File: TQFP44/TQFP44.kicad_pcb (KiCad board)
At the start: 2 copper layers, 56.1 x 20.6 mm, 12 parts, among them J1 Conn_01x22, J2 Conn_01x22, J3 Conn_02x22_Counter_Clockwise, J4 Conn_02x22_Counter_Clockwise, J5 Conn_02x22_Counter_Clockwise, J6 Conn_01x06

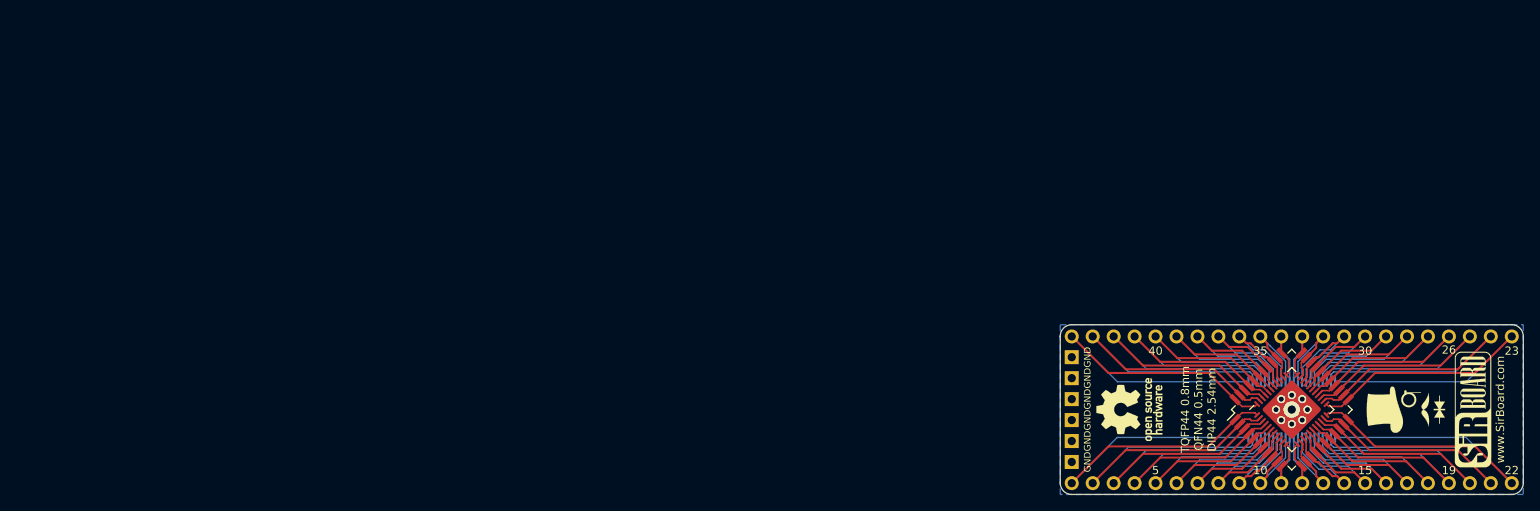
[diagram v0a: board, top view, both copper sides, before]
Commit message: USB, SD and CR Cells Added
MicroSD, MicroUSB, MiniUSB, USB-C, CR1220, CR2032 added as well as all schematics page sizes optimised
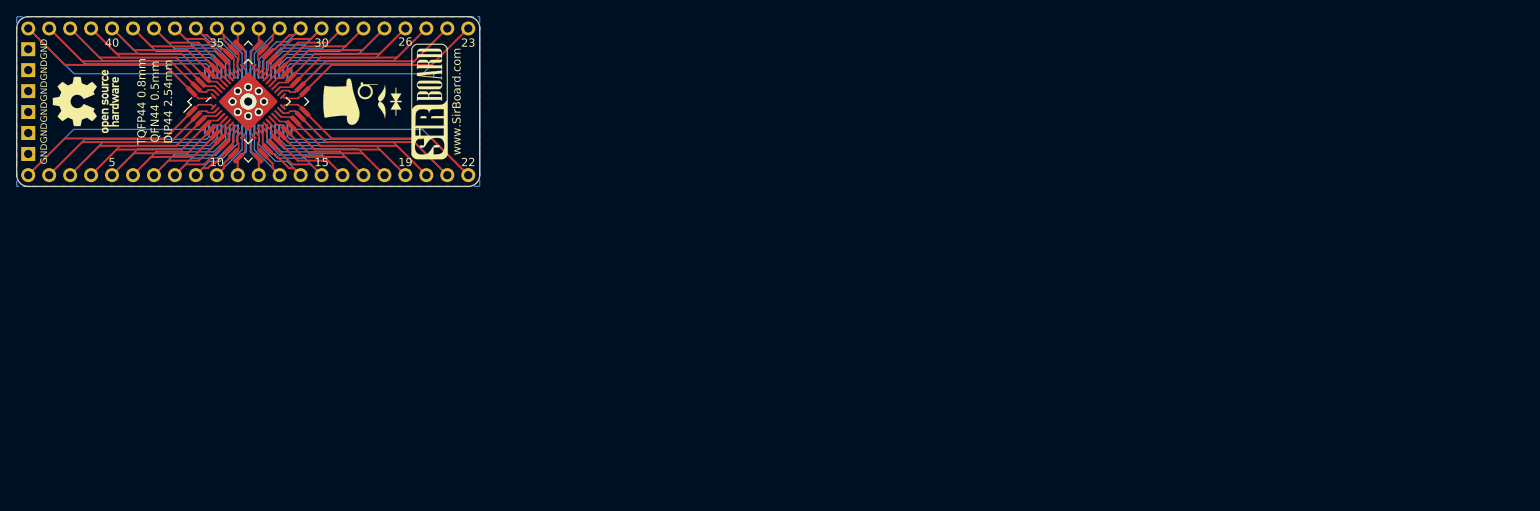
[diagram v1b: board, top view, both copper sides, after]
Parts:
- moved J3 131.9 mm to (67.9, 35.1)
- moved J5 131.9 mm to (67.9, 35.1)
- moved REF** 131.9 mm to (48.3, 35.1)
- moved G*** 131.9 mm to (81.8, 35.1)
- moved G*** 131.9 mm to (89.2, 35.1)
- moved G*** 131.9 mm to (79.4, 35.0)
- moved G*** 131.9 mm to (89.9, 35.1)
- moved J1 131.9 mm to (41.3, 26.2)
- moved J2 131.9 mm to (41.3, 44.0)
- moved J4 131.9 mm to (67.9, 35.0)
- moved J6 131.9 mm to (41.3, 41.4)
- moved REF** 131.9 mm to (50.7, 35.1)

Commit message: Board Updates
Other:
- board size 56.1 x 20.6 mm -> 55.9 x 20.3 mm
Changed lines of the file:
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@@
     (0 F.Cu signal)
     (31 B.Cu signal)
-    (32 B.Adhes user)
-    (33 F.Adhes user)
-    (34 B.Paste user)
-    (35 F.Paste user)
+    (32 B.Adhes user hide)
+    (33 F.Adhes user hide)
+    (34 B.Paste user hide)
+    (35 F.Paste user hide)
     (36 B.SilkS user)
     (37 F.SilkS user)
-    (38 B.Mask user)
-    (39 F.Mask user)
+    (38 B.Mask user hide)
+    (39 F.Mask user hide)
     (40 Dwgs.User user)
     (41 Cmts.User user hide)
@@
       (xy -6.38175 -2.199822) (xy 6.399893 -2.199822) (xy 6.472464 -2.17505)) (layer F.SilkS) (width 0.01))
   )
+  (gr_arc (start 94.615 43.942) (end 94.615 45.212) (angle -90) (layer Edge.Cuts) (width 0.05))
+  (gr_arc (start 41.275 43.942) (end 40.005 43.942) (angle -90) (layer Edge.Cuts) (width 0.05))
+  (gr_arc (start 41.275 26.162) (end 41.275 24.892) (angle -90) (layer Edge.Cuts) (width 0.05))
+  (gr_arc (start 94.615 26.162) (end 95.885 26.162) (angle -90) (layer Edge.Cuts) (width 0.05))
   (gr_text 44 (at 94.615 27.813) (layer B.SilkS)
     (effects (font (size 1 1) (thickness 0.15)) (justify mirror))
@@
     (effects (font (size 1 1) (thickness 0.15)) (justify mirror))
   )
-  (dimension 56.134 (width 0.15) (layer Dwgs.User)
-    (gr_text "56.134 mm" (at 67.945 18.6898) (layer Dwgs.User)
+  (dimension 55.88 (width 0.15) (layer Dwgs.User)
+    (gr_text "55.880 mm" (at 67.945 18.766) (layer Dwgs.User)
       (effects (font (size 1 1) (thickness 0.15)) hide)
     )
-    (feature1 (pts (xy 96.012 24.765) (xy 96.012 19.403379)))
-    (feature2 (pts (xy 39.878 24.765) (xy 39.878 19.403379)))
-    (crossbar (pts (xy 39.878 19.9898) (xy 96.012 19.9898)))
-    (arrow1a (pts (xy 96.012 19.9898) (xy 94.885496 20.576221)))
-    (arrow1b (pts (xy 96.012 19.9898) (xy 94.885496 19.403379)))
-    (arrow2a (pts (xy 39.878 19.9898) (xy 41.004504 20.576221)))
-    (arrow2b (pts (xy 39.878 19.9898) (xy 41.004504 19.403379)))
+    (feature1 (pts (xy 95.885 26.162) (xy 95.885 19.479579)))
+    (feature2 (pts (xy 40.005 26.162) (xy 40.005 19.479579)))
+    (crossbar (pts (xy 40.005 20.066) (xy 95.885 20.066)))
+    (arrow1a (pts (xy 95.885 20.066) (xy 94.758496 20.652421)))
+    (arrow1b (pts (xy 95.885 20.066) (xy 94.758496 19.479579)))
+    (arrow2a (pts (xy 40.005 20.066) (xy 41.131504 20.652421)))
+    (arrow2b (pts (xy 40.005 20.066) (xy 41.131504 19.479579)))
   )
-  (dimension 20.574 (width 0.15) (layer Dwgs.User)
-    (gr_text "20.574 mm" (at 33.955298 35.052 270) (layer Dwgs.User)
+  (dimension 20.32 (width 0.15) (layer Dwgs.User)
+    (gr_text "20.320 mm" (at 34.387 35.052 270) (layer Dwgs.User)
       (effects (font (size 1 1) (thickness 0.15)) hide)
     )
-    (feature1 (pts (xy 39.878 45.339) (xy 34.668877 45.339)))
-    (feature2 (pts (xy 39.878 24.765) (xy 34.668877 24.765)))
-    (crossbar (pts (xy 35.255298 24.765) (xy 35.255298 45.339)))
-    (arrow1a (pts (xy 35.255298 45.339) (xy 34.668877 44.212496)))
-    (arrow1b (pts (xy 35.255298 45.339) (xy 35.841719 44.212496)))
-    (arrow2a (pts (xy 35.255298 24.765) (xy 34.668877 25.891504)))
-    (arrow2b (pts (xy 35.255298 24.765) (xy 35.841719 25.891504)))
+    (feature1 (pts (xy 41.275 45.212) (xy 35.100579 45.212)))
+    (feature2 (pts (xy 41.275 24.892) (xy 35.100579 24.892)))
+    (crossbar (pts (xy 35.687 24.892) (xy 35.687 45.212)))
+    (arrow1a (pts (xy 35.687 45.212) (xy 35.100579 44.085496)))
+    (arrow1b (pts (xy 35.687 45.212) (xy 36.273421 44.085496)))
+    (arrow2a (pts (xy 35.687 24.892) (xy 35.100579 26.018504)))
+    (arrow2b (pts (xy 35.687 24.892) (xy 36.273421 26.018504)))
   )
   (dimension 17.78 (width 0.15) (layer Dwgs.User)
@@
     (arrow2b (pts (xy 41.275 22.6822) (xy 42.401504 22.095779)))
   )
-  (gr_arc (start 41.275 43.942) (end 39.878 43.942) (angle -90) (layer Edge.Cuts) (width 0.05))
-  (gr_arc (start 94.615 43.942) (end 94.615 45.339) (angle -90) (layer Edge.Cuts) (width 0.05))
-  (gr_arc (start 94.615 26.162) (end 96.012 26.162) (angle -90) (layer Edge.Cuts) (width 0.05))
-  (gr_arc (start 41.275 26.162) (end 41.275 24.765) (angle -90) (layer Edge.Cuts) (width 0.05))
   (gr_circle (center 67.944577 35.052) (end 68.6816 35.052) (layer B.Mask) (width 0.5))
   (gr_circle (center 67.944577 35.052) (end 68.6816 35.052) (layer F.Mask) (width 0.5))
@@
     (effects (font (size 1 1) (thickness 0.15)))
   )
-  (gr_line (start 96.012 43.942) (end 96.012 26.162) (layer Edge.Cuts) (width 0.05))
-  (gr_line (start 41.275 45.339) (end 94.615 45.339) (layer Edge.Cuts) (width 0.05))
-  (gr_line (start 39.878 26.162) (end 39.878 43.942) (layer Edge.Cuts) (width 0.05))
-  (gr_line (start 94.615 24.765) (end 41.275 24.765) (layer Edge.Cuts) (width 0.05))
+  (gr_line (start 95.885 43.942) (end 95.885 26.162) (layer Edge.Cuts) (width 0.05))
+  (gr_line (start 41.275 45.212) (end 94.615 45.212) (layer Edge.Cuts) (width 0.05))
+  (gr_line (start 40.005 26.162) (end 40.005 43.942) (layer Edge.Cuts) (width 0.05))
+  (gr_line (start 94.615 24.892) (end 41.275 24.892) (layer Edge.Cuts) (width 0.05))
   (segment (start 72.143447 34.389087) (end 72.42536 34.671) (width 0.2) (layer F.Cu) (net 1))
   (segment (start 73.982854 34.671) (end 74.803936 33.849918) (width 0.2) (layer F.Cu) (net 1))
@@
     (polygon
       (pts
-        (xy 39.878 24.765) (xy 96.012 24.765) (xy 96.012 45.339) (xy 39.878 45.339)
+        (xy 40.005 24.892) (xy 95.885 24.892) (xy 95.885 45.212) (xy 40.005 45.212)
       )
     )

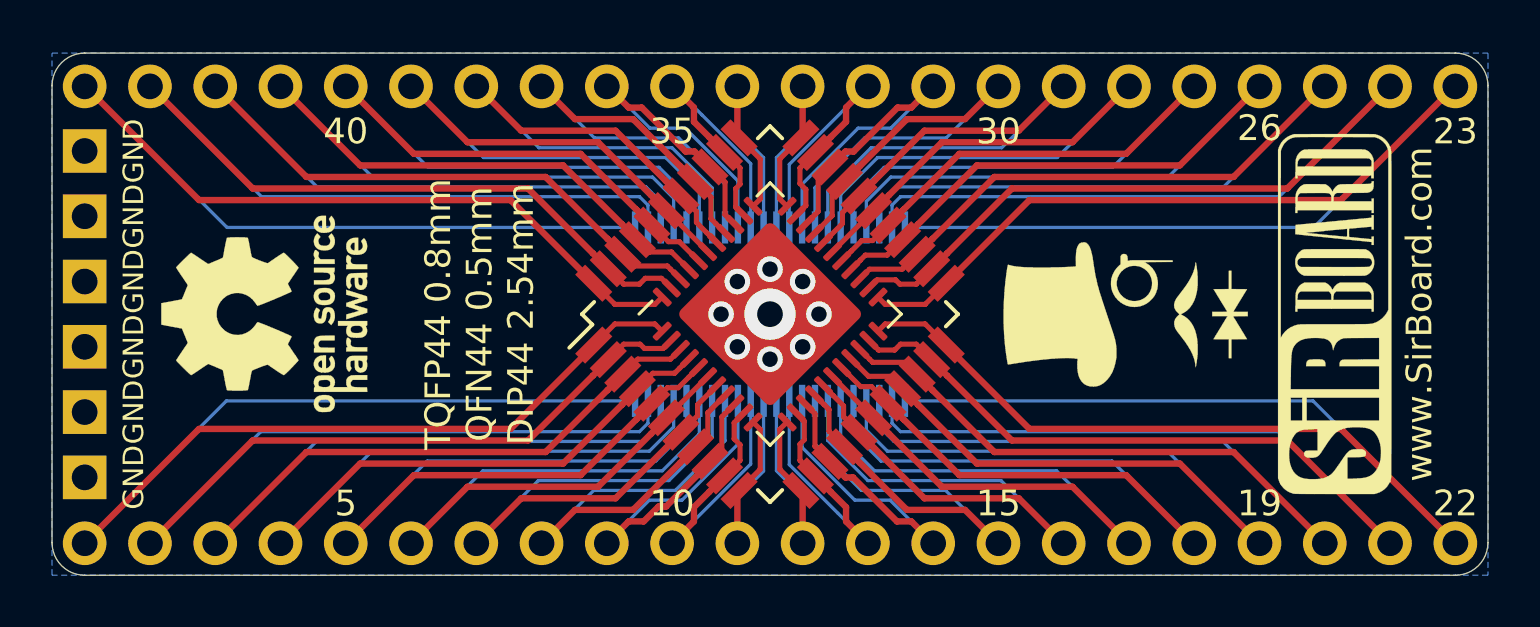
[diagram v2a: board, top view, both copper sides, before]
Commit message: Breakout Boards Revision 2
Renders updated, silkscreen text improved, blurry silkscreen items removed/resized.
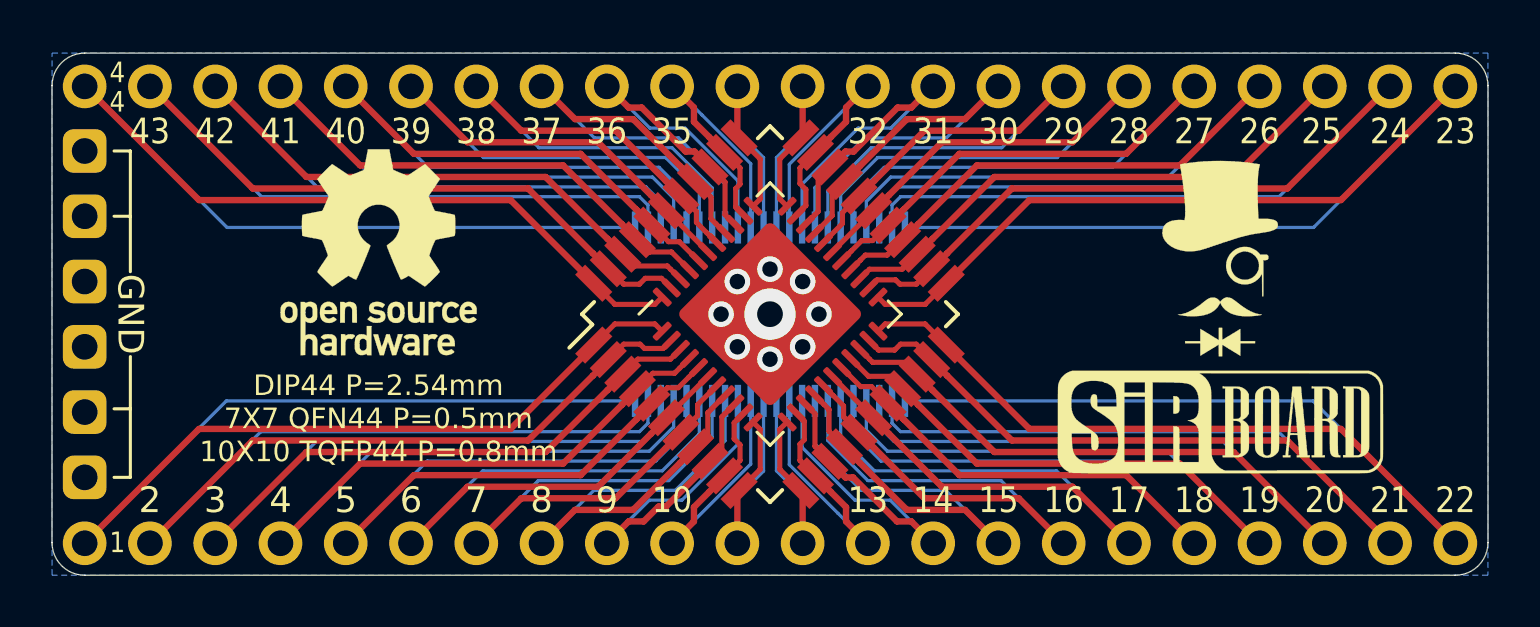
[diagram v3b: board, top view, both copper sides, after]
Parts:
- removed the G*** at (89.2, 35.1)
- removed the G*** at (79.4, 35.0)
- added G***: LOGO, logo:SirBoard127x40, B.Cu at (51.8, 39.1)
- added G***: LOGO, logo:logo76x107, B.Cu at (51.8, 32.8)
- G***: footprint logo:SirBoard140x44 -> logo:SirBoard127x40
- G***: footprint logo:logo94x134 -> logo:logo76x107
- moved REF** 34.2 mm to (84.8, 33.5), turned to 180 degrees
- moved G*** 6.11 mm to (85.5, 39.2), turned to 0 degrees
- moved REF** 5.06 mm to (52.7, 32.6), turned to 0 degrees
- moved G*** 4.27 mm to (85.5, 32.9), turned to 0 degrees
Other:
- board text added: "11"
- board text added: "12"
- board text added: "13"
- board text added: "14"
- board text added: "16"
- board text added: "17"
- board text added: "18"
- board text added: "2"
- board text added: "20"
- board text added: "21"
- board text added: "24"
- board text added: "25"
- board text added: "27"
- board text added: "28"
- board text added: "29"
- board text added: "3"
- board text added: "31"
- board text added: "32"
- board text added: "33"
- board text added: "34"
- board text added: "36"
- board text added: "37"
- board text added: "38"
- board text added: "39"
- board text added: "4"
- board text added: "41"
- board text added: "42"
- board text added: "43"
- board text added: "6"
- board text added: "7"
- board text added: "8"
- board text added: "9"
- board text added: "DIP44 P=2.54mm 7X7 QFN44 P=0.5mm 10X10 TQFP44 P=0.8mm"
- board text removed: "TQFP44 0.8mm QFN44 0.5mm DIP44 2.54mm"
